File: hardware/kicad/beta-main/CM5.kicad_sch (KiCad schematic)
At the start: 2 parts, among them J1 FFC3A20-15-G, J2 FFC3A20-15-G

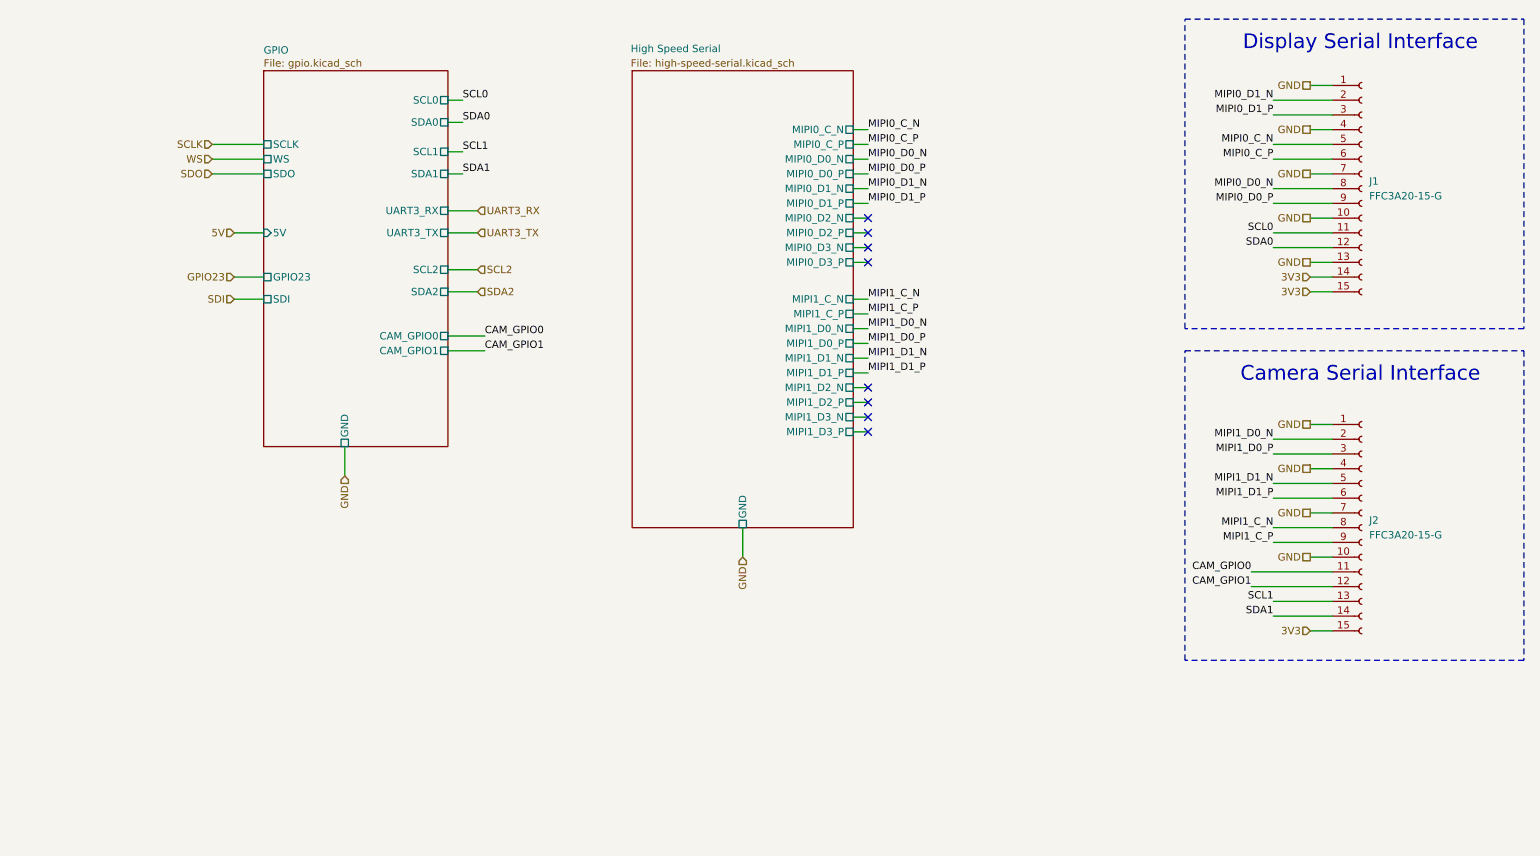
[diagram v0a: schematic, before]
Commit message: remove power symbols from hierarchy and move different subsystems  around
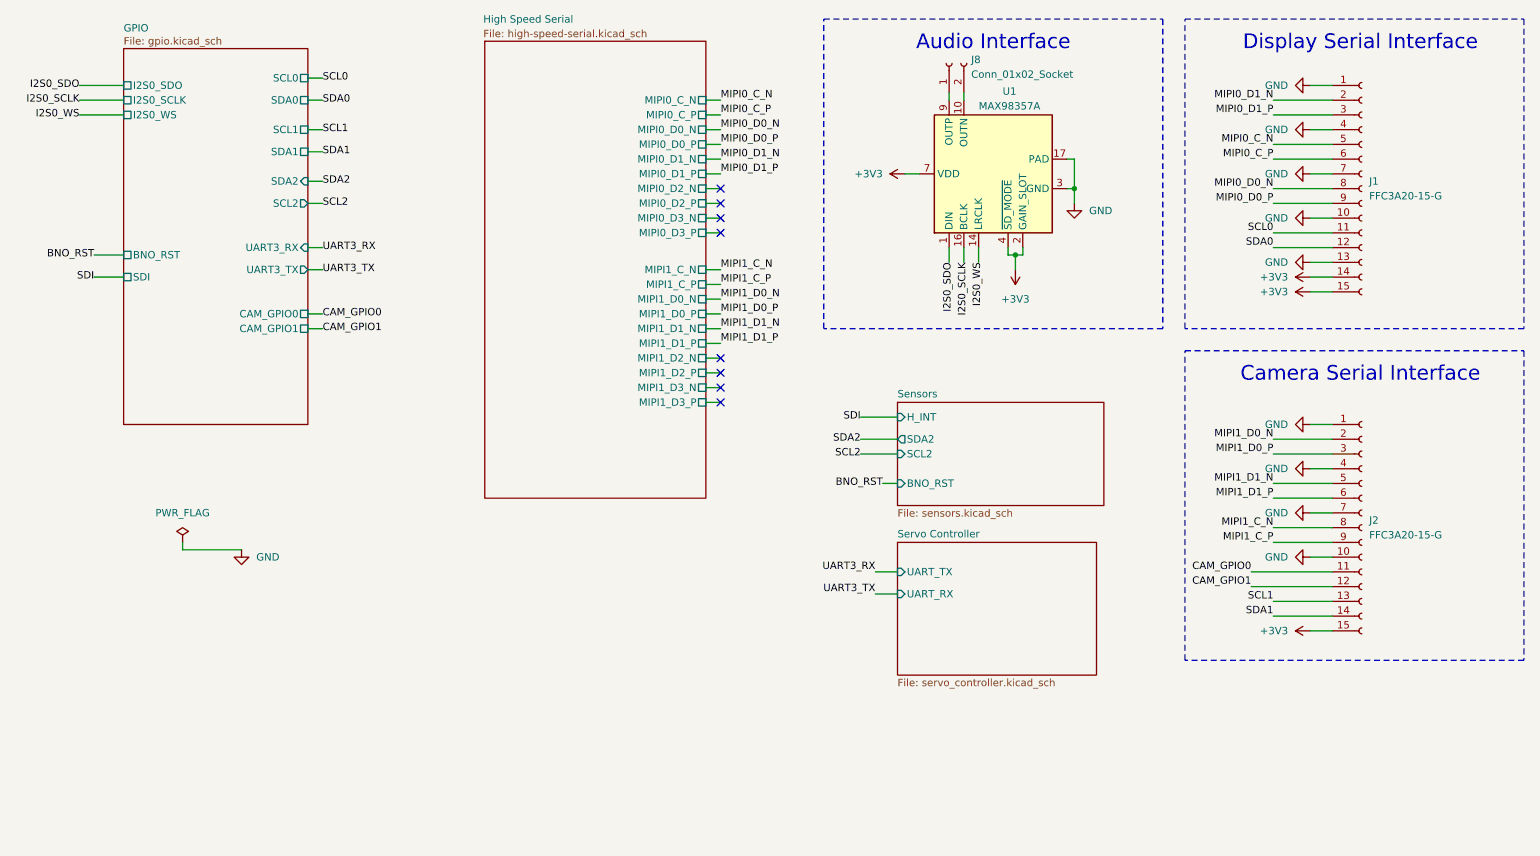
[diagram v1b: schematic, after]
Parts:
- added J8: Conn_01x02_Socket, Connector_PinHeader_2.54mm:PinHeader_1x02_P2.54mm_Vertical, symbol Connector:Conn_01x02_Socket
- added U1: MAX98357A, Package_DFN_QFN:TQFN-16-1EP_3x3mm_P0.5mm_EP1.23x1.23mm, symbol Audio:MAX98357A
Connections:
- net GND: now also U1.11 (GND), U1.15 (GND), U1.17 (PAD), U1.3 (GND)
- net 3V3 renamed +3V3
- net +3V3: now also U1.2 (GAIN_SLOT), U1.4 (~{SD_MODE}), U1.7 (VDD), U1.8 (VDD)
- new net: J8.2 (Pin_2), U1.10 (OUTN)
- new net: J8.1 (Pin_1), U1.9 (OUTP)
- new net I2S0_SCLK: U1.16 (BCLK)
- new net I2S0_SDO: U1.1 (DIN)
- new net I2S0_WS: U1.14 (LRCLK)
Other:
- added sheet Sensors (sensors.kicad_sch)
- added sheet Servo Controller (servo_controller.kicad_sch)
- sheet GPIO ports: added BNO_RST, I2S0_SCLK, I2S0_SDO, I2S0_WS; removed 5V, GND, GPIO23, SCLK, SDO, WS
- sheet High Speed Serial ports: added none; removed GND
- note added: "Audio Interface"

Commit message: use copied MAX98357 symbol to specify pin type
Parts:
- U1: symbol Audio:MAX98357A -> Beta:MAX98357A

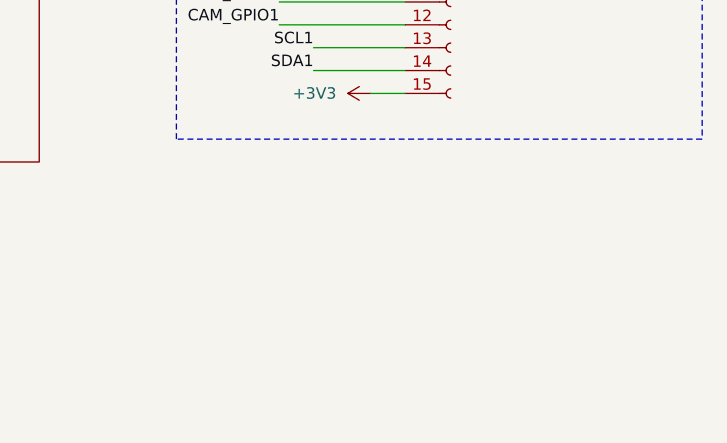
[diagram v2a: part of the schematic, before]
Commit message: Footprints fixed, fuse removed
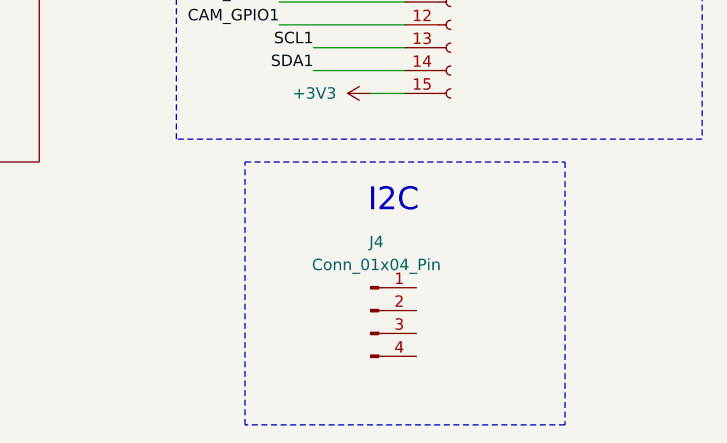
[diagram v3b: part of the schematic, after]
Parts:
- added J4: Conn_01x04_Pin, Connector_JST:JST_XH_B4B-XH-AM_1x04_P2.50mm_Vertical, symbol Connector:Conn_01x04_Pin
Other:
- note added: "I2C"
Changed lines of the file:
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@@
+	)
+	(rectangle
+		(start 223.52 130.81)
+		(end 259.08 160.02)
+		(stroke
+			(width 0)
+			(type dash)
+		)
+		(fill
+			(type none)
+		)
 	)
 	(rectangle
@@
 		(exclude_from_sim no)
 		(at 246.126 78.994 0)
+		(effects
+			(font
+				(size 2.54 2.54)
+			)
+		)
+	)
+	(text "I2C"
+		(exclude_from_sim no)
+		(at 240.03 135.128 0)
 		(effects
 			(font
@@
 					(unit 1)
 				)
+			)
+		)
+	)
+	(symbol
+		(lib_id "Connector:Conn_01x04_Pin")
+		(at 237.49 147.32 0)
+		(unit 1)
+		(exclude_from_sim no)
+		(in_bom yes)
+		(on_board yes)
+		(dnp no)
+		(fields_autoplaced yes)
+		(property "Reference" "J4"
+			(at 238.125 139.7 0)
+			(effects
+				(font
+					(size 1.27 1.27)
+				)
+			)
+		)
+		(property "Value" "Conn_01x04_Pin"
+			(at 238.125 142.24 0)
+			(effects
+				(font
+					(size 1.27 1.27)
+				)
+			)
+		)
+		(property "Footprint" "Connector_JST:JST_XH_B4B-XH-AM_1x04_P2.50mm_Vertical"
+			(at 237.49 147.32 0)
+			(effects
+				(font
+					(size 1.27 1.27)
+				)
+				(hide yes)
+			)
+		)
+		(property "Datasheet" "~"
+			(at 237.49 147.32 0)
+			(effects
+				(font
+					(size 1.27 1.27)
+				)
+				(hide yes)
+			)
+		)
+		(property "Description" "Generic connector, single row, 01x04, script generated"
+			(at 237.49 147.32 0)
+			(effects
+				(font
+					(size 1.27 1.27)
+				)
+				(hide yes)
+			)
+		)
+		(pin "4"
+		)
+		(pin "2"
+		)
+		(pin "3"
+		)
+		(pin "1"
+		)
+		(instances
+			(project ""
+				(path "/ec75fd42-4efa-4f32-b57e-76d632cb46f5/b3cf40a7-4d41-420e-a440-2c08f4160b31"
+					(reference "J4")
+					(unit 1)
+				)
